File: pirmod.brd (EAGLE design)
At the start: 17.8 x 17.8 mm, 13 parts, among them IC2 TLC555, J1 22V, J2 GND, J3 TACT, J4 OUT-PIR, J5 OUT

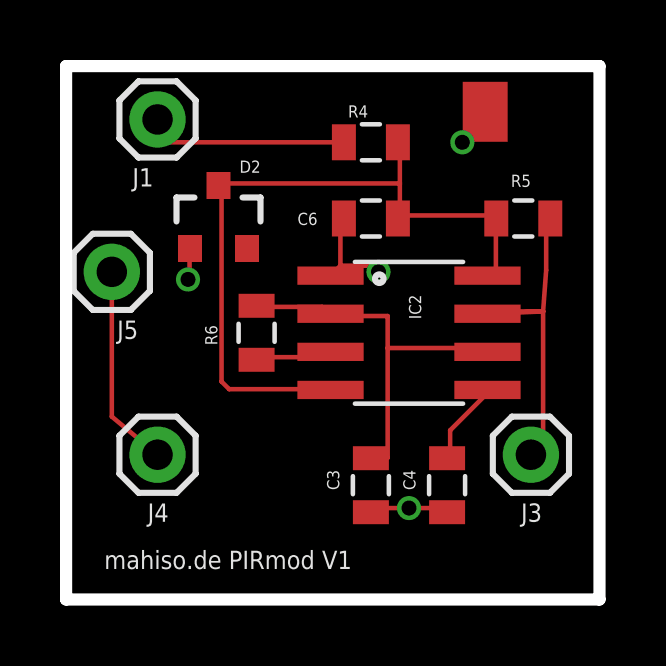
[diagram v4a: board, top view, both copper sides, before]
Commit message: Bauteilnummerierung geändert.
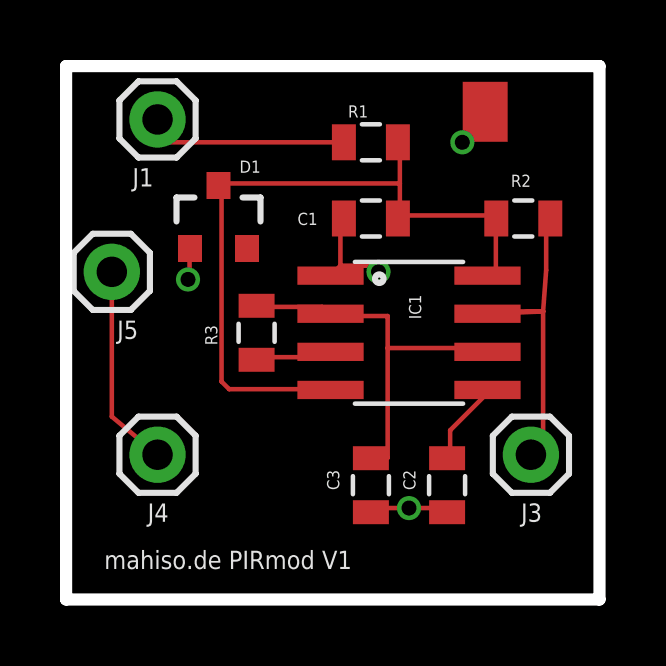
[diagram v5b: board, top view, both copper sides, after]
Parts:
- renumbered C4 to C2, C6 to C1, D2 to D1, IC2 to IC1, R4 to R1, R5 to R2, R6 to R3
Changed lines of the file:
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@@
 <attribute name="VALUE" x="8.763" y="4.826" size="0.4064" layer="27" rot="R270"/>
 </element>
-<element name="C4" library="SparkFun-Capacitors" package="0805" value="100n" x="12.7" y="3.81" smashed="yes" rot="R270">
+<element name="C2" library="SparkFun-Capacitors" package="0805" value="100n" x="12.7" y="3.81" smashed="yes" rot="R270">
 <attribute name="NAME" x="11.2395" y="4.318" size="0.4064" layer="25" rot="R270"/>
 <attribute name="VALUE" x="11.303" y="4.826" size="0.4064" layer="27" rot="R270"/>
 </element>
-<element name="C6" library="SparkFun-Capacitors" package="0805" value="100n" x="10.16" y="12.7" smashed="yes" rot="R180">
+<element name="C1" library="SparkFun-Capacitors" package="0805" value="100n" x="10.16" y="12.7" smashed="yes" rot="R180">
 <attribute name="NAME" x="8.382" y="12.8905" size="0.4064" layer="25" rot="R180"/>
 <attribute name="VALUE" x="11.176" y="14.097" size="0.4064" layer="27" rot="R180"/>
 </element>
-<element name="D2" library="SparkFun-DiscreteSemi" package="SOT23-3" value="BCX84-C12" x="5.08" y="12.7" smashed="yes">
+<element name="D1" library="SparkFun-DiscreteSemi" package="SOT23-3" value="BCX84-C12" x="5.08" y="12.7" smashed="yes">
 <attribute name="NAME" x="5.7785" y="14.224" size="0.4064" layer="25"/>
 <attribute name="VALUE" x="4.064" y="12.5095" size="0.4064" layer="27"/>
 </element>
-<element name="IC2" library="SparkFun-AnalogIC" package="SO08" value="TLC555" x="11.43" y="8.89" rot="R270"/>
+<element name="IC1" library="SparkFun-AnalogIC" package="SO08" value="TLC555" x="11.43" y="8.89" rot="R270"/>
 <element name="J1" library="SparkFun-Connectors" package="1X01" value="22V" x="3.048" y="16.002" smashed="yes">
 <attribute name="NAME" x="2.2098" y="13.7668" size="0.6096" layer="25"/>
@@
 <attribute name="VALUE" x="0.254" y="7.747" size="0.6096" layer="27"/>
 </element>
-<element name="R4" library="SparkFun-Passives" package="0805" value="2,2k" x="10.16" y="15.24"/>
-<element name="R5" library="SparkFun-Passives" package="0805" value="4,7k" x="15.24" y="12.7" smashed="yes" rot="R180">
+<element name="R1" library="SparkFun-Passives" package="0805" value="2,2k" x="10.16" y="15.24"/>
+<element name="R2" library="SparkFun-Passives" package="0805" value="4,7k" x="15.24" y="12.7" smashed="yes" rot="R180">
 <attribute name="NAME" x="15.494" y="14.1605" size="0.4064" layer="25" rot="R180"/>
 <attribute name="VALUE" x="16.256" y="14.097" size="0.4064" layer="27" rot="R180"/>
 </element>
-<element name="R6" library="SparkFun-Passives" package="0805" value="27k" x="6.35" y="8.89" smashed="yes" rot="R270">
+<element name="R3" library="SparkFun-Passives" package="0805" value="27k" x="6.35" y="8.89" smashed="yes" rot="R270">
 <attribute name="NAME" x="4.6355" y="9.144" size="0.4064" layer="25" rot="R270"/>
 <attribute name="VALUE" x="4.953" y="9.906" size="0.4064" layer="27" rot="R270"/>
@@
 <signals>
 <signal name="GND">
-<contactref element="C4" pad="2"/>
+<contactref element="C2" pad="2"/>
 <contactref element="C3" pad="2"/>
-<contactref element="IC2" pad="1"/>
-<contactref element="C6" pad="2"/>
-<contactref element="D2" pad="1"/>
+<contactref element="IC1" pad="1"/>
+<contactref element="C1" pad="2"/>
+<contactref element="D1" pad="1"/>
 <contactref element="J2" pad="P$1"/>
 <polygon width="0.4064" layer="16">
@@
 </signal>
 <signal name="N$3">
-<contactref element="IC2" pad="6"/>
-<contactref element="IC2" pad="2"/>
+<contactref element="IC1" pad="6"/>
+<contactref element="IC1" pad="2"/>
 <contactref element="C3" pad="1"/>
-<contactref element="R6" pad="1"/>
+<contactref element="R3" pad="1"/>
 <wire x1="10.7188" y1="9.4488" x2="10.7188" y2="8.382" width="0.1524" layer="1"/>
 <wire x1="10.7188" y1="8.382" x2="10.7188" y2="4.7244" width="0.1524" layer="1"/>
@@
 </signal>
 <signal name="N$7">
-<contactref element="IC2" pad="5"/>
-<contactref element="C4" pad="1"/>
+<contactref element="IC1" pad="5"/>
+<contactref element="C2" pad="1"/>
 <wire x1="12.8016" y1="5.6388" x2="12.8016" y2="4.7244" width="0.1524" layer="1"/>
 <wire x1="14.0208" y1="6.858" x2="12.8016" y2="5.6388" width="0.1524" layer="1"/>
@@
 </signal>
 <signal name="N$8">
-<contactref element="R6" pad="2"/>
-<contactref element="IC2" pad="3"/>
+<contactref element="R3" pad="2"/>
+<contactref element="IC1" pad="3"/>
 <wire x1="8.5344" y1="8.0772" x2="6.4008" y2="8.0772" width="0.1524" layer="1"/>
 <wire x1="8.6868" y1="8.2296" x2="8.5344" y2="8.0772" width="0.1524" layer="1"/>
@@
 </signal>
 <signal name="N$9">
-<contactref element="IC2" pad="7"/>
-<contactref element="R5" pad="1"/>
+<contactref element="IC1" pad="7"/>
+<contactref element="R2" pad="1"/>
 <contactref element="J3" pad="1"/>
 <wire x1="16.002" y1="10.9728" x2="16.002" y2="12.6492" width="0.1524" layer="1"/>
@@
 </signal>
 <signal name="12V">
-<contactref element="R4" pad="2"/>
-<contactref element="D2" pad="3"/>
-<contactref element="R5" pad="2"/>
-<contactref element="C6" pad="1"/>
-<contactref element="IC2" pad="8"/>
-<contactref element="IC2" pad="4"/>
+<contactref element="R1" pad="2"/>
+<contactref element="D1" pad="3"/>
+<contactref element="R2" pad="2"/>
+<contactref element="C1" pad="1"/>
+<contactref element="IC1" pad="8"/>
+<contactref element="IC1" pad="4"/>
 <wire x1="14.3256" y1="10.9728" x2="14.3256" y2="12.6492" width="0.1524" layer="1"/>
 <wire x1="14.1732" y1="10.8204" x2="14.3256" y2="10.9728" width="0.1524" layer="1"/>
@@
 </signal>
 <signal name="N$5">
-<contactref element="R4" pad="1"/>
+<contactref element="R1" pad="1"/>
 <contactref element="J1" pad="1"/>
 <wire x1="3.3528" y1="15.24" x2="9.26" y2="15.24" width="0.1524" layer="1"/>
